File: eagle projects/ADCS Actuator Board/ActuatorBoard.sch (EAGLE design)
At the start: 256 parts, among them J4 OSTVN08A150, J5 OSTVN08A150, J6 OSTVN08A150, U10 TVS991, U11 BD621F-E2, U12 ADS7841E_2K5, U13 ADS7841E_2K5, U15 TLV9051IDCKR, U16 BD621F-E2, U17 DRV10970_MOTOR_DRIVERDRV10970, U18 DRV10970_MOTOR_DRIVERDRV10970, U19 TLV9051IDCKR, U20 DRV10970_MOTOR_DRIVERDRV10970, U21 TLV9051IDCKR, U22 BD621F-E2, U23 TLV9051IDCKR, U24 TLV9051IDCKR, U25 ADS7841E_2K5, U26 TLV9051IDCKR, U27 ADS7841E_2K5, U28 TLV9051IDCKR, U29 TLV9051IDCKR, U30 TLV9051IDCKR, U31 TLV9051IDCKR, U32 TLV9051IDCKR, U4 ADS7841E_2K5, U6 TLV9051IDCKR, U7 TVS991, U8 TVS991, U9 ADS7841E_2K5

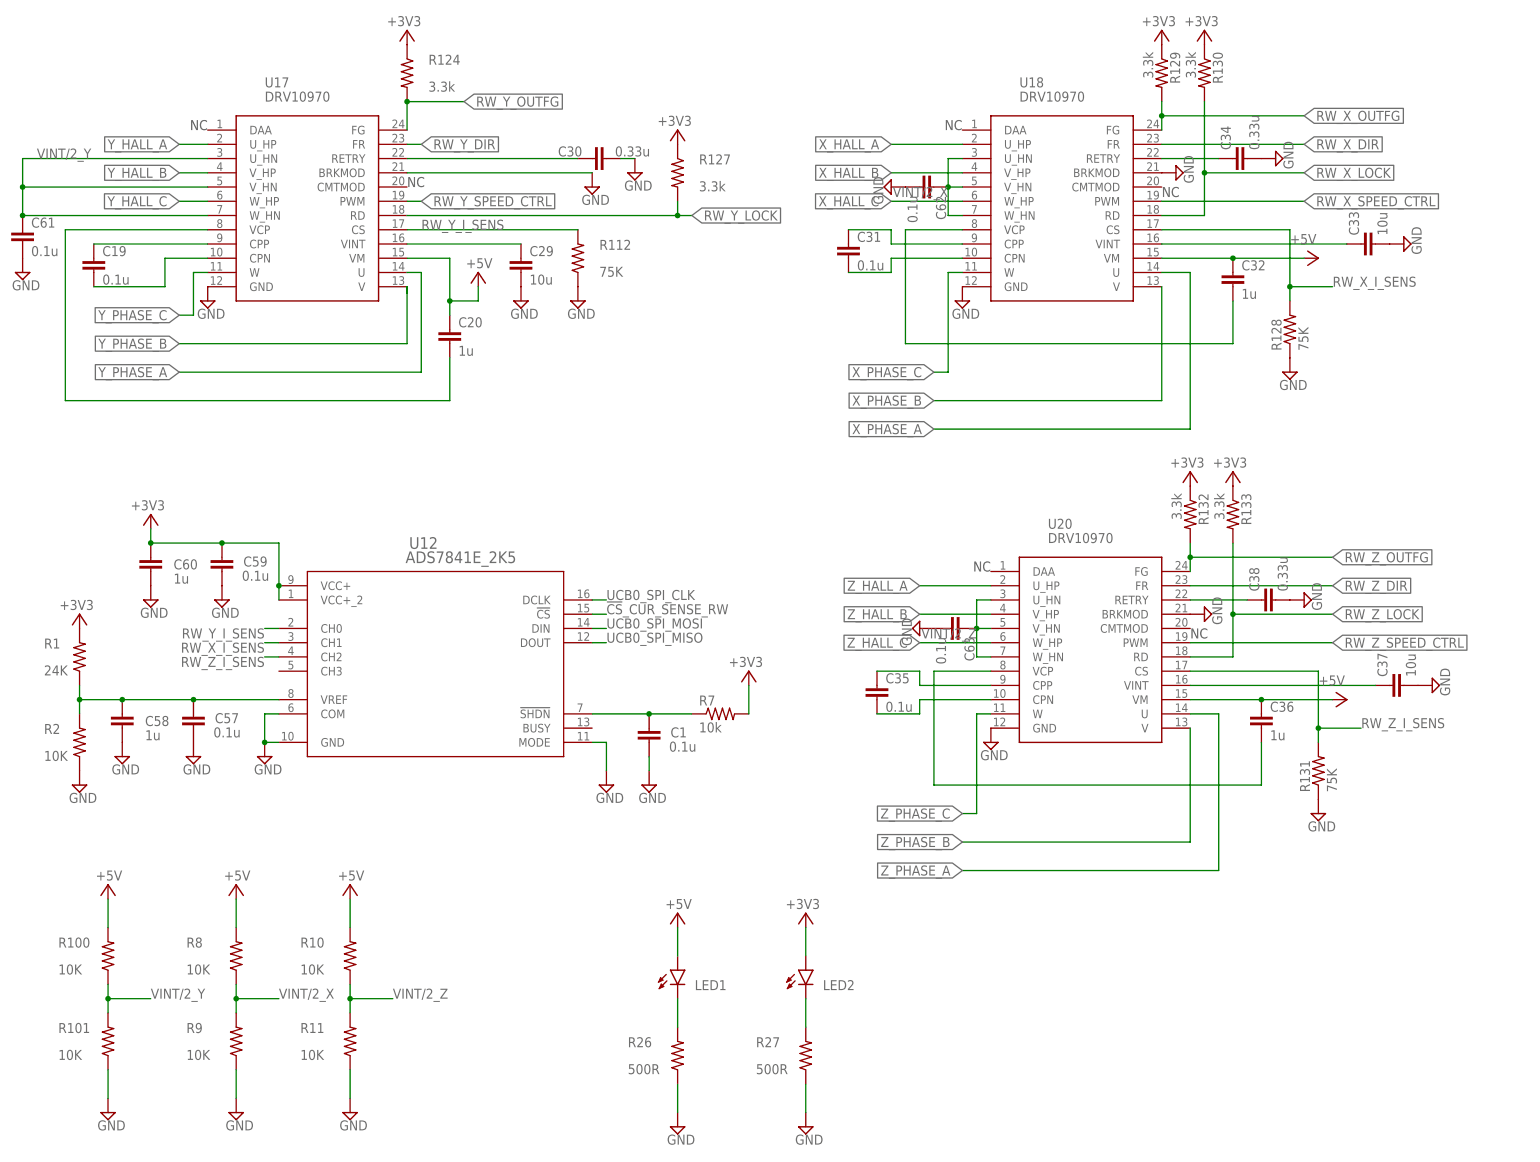
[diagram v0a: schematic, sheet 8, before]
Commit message: replaced 10u caps with 4.7u
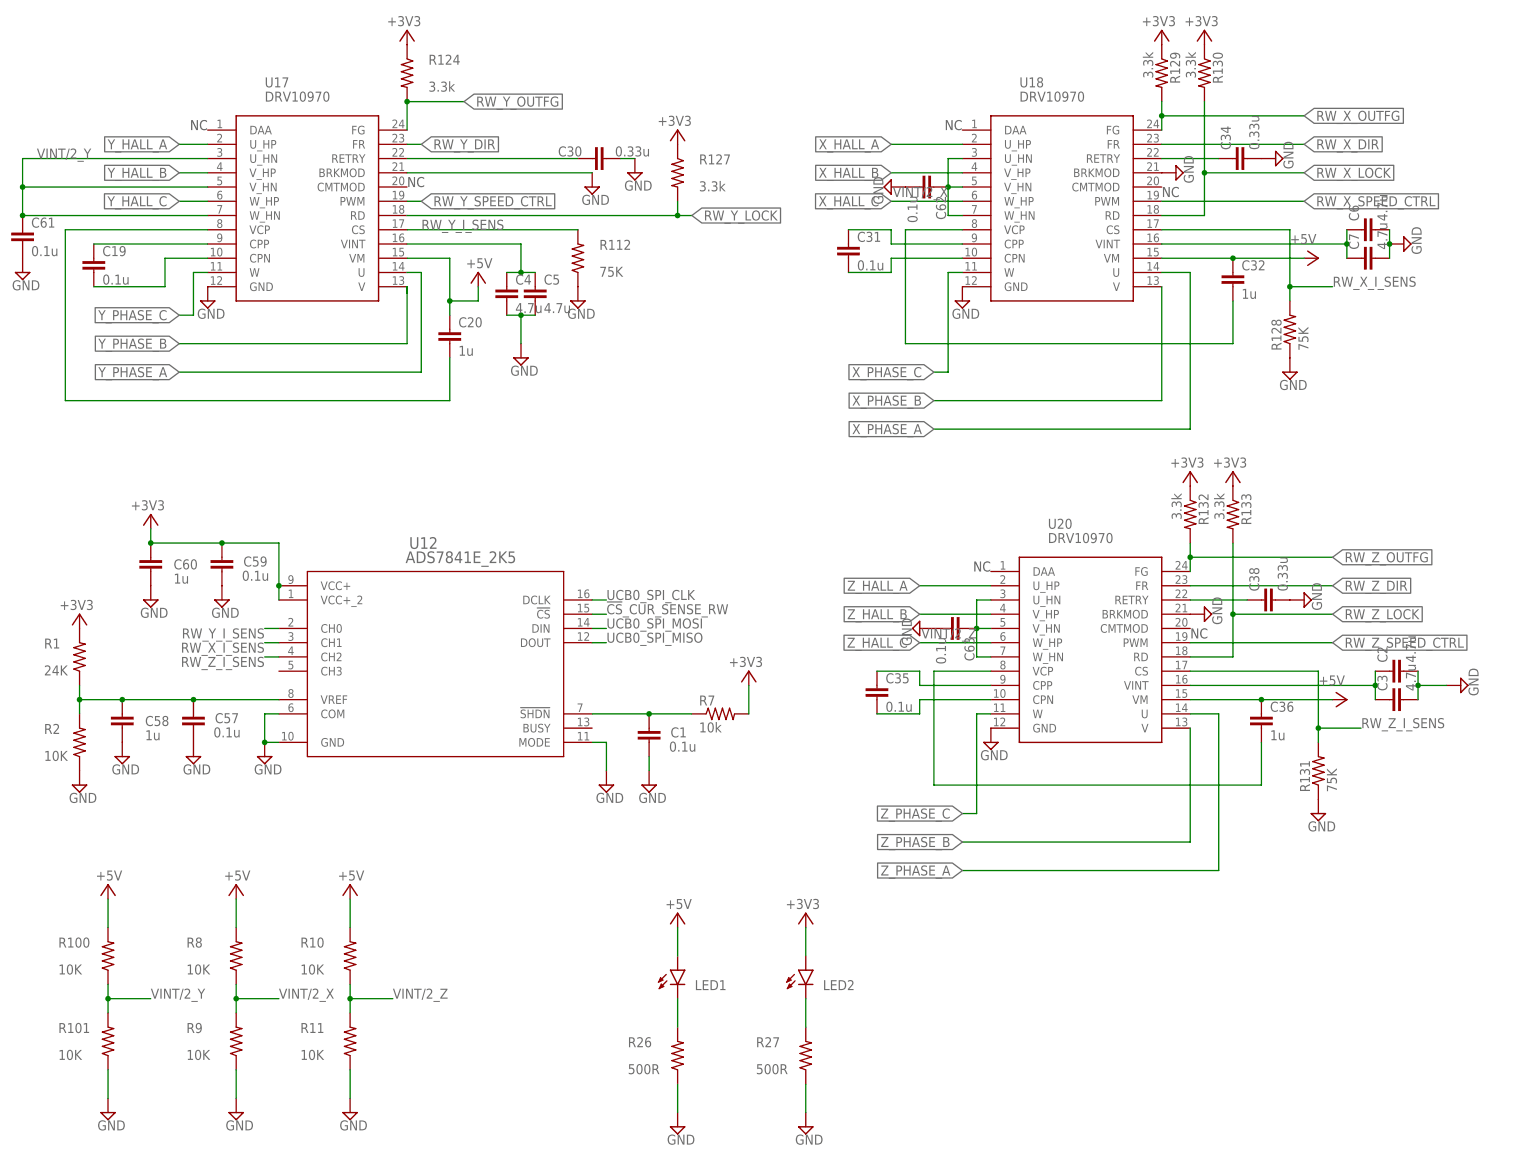
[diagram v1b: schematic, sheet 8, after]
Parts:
- removed C29, C33, C37: 10u, rcl:C-EUC0603
- added C2, C3, C4, C5, C6, C7: 4.7u, resistor:C-EUC0402
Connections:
- removed net N$28: J2.15
- net +3V3: now also J2.15
- net GND: now also C2.2, C3.2, C4.2, C5.2, C6.2, C7.2; no longer C29.2, C33.2, C37.2
- net N$26: now also C4.1, C5.1; no longer C29.1
- net N$42: now also C6.1, C7.1; no longer C33.1
- net N$53: now also C2.1, C3.1; no longer C37.1

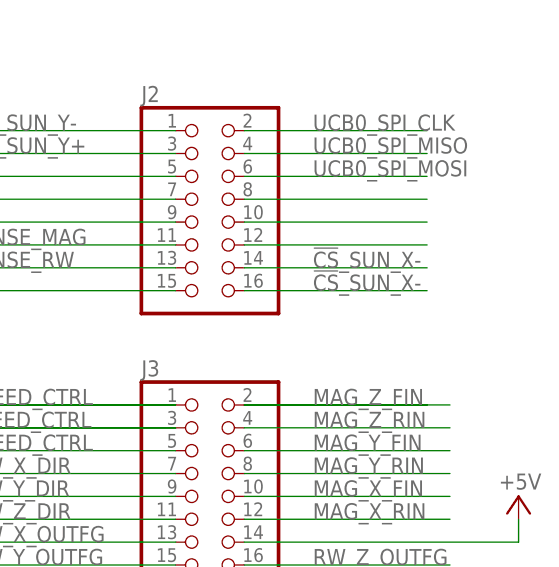
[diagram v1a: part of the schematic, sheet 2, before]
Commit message: laid out polygons for power plane
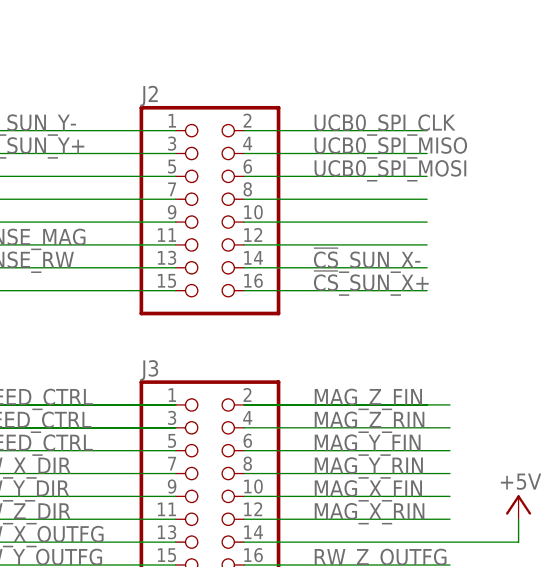
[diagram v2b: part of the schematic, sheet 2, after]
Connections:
- net !CS!_SUN_X+: now also J2.16
- net !CS!_SUN_X-: no longer J2.16
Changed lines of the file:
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@@
 <net name="!CS!_SUN_X-" class="0">
-<segment>
-<wire x1="185.42" y1="119.38" x2="165.1" y2="119.38" width="0.1524" layer="91" grouprefs="SENSOR_BOARD_CONNNECTOR"/>
-<pinref part="J2" gate="A" pin="16"/>
-<label x="172.72" y="119.38" size="1.778" layer="95" grouprefs="SENSOR_BOARD_CONNNECTOR"/>
-</segment>
 <segment>
 <pinref part="J2" gate="A" pin="14"/>
@@
 </segment>
 </net>
+<net name="!CS!_SUN_X+" class="0">
+<segment>
+<wire x1="185.42" y1="119.38" x2="165.1" y2="119.38" width="0.1524" layer="91" grouprefs="SENSOR_BOARD_CONNNECTOR"/>
+<pinref part="J2" gate="A" pin="16"/>
+<label x="172.72" y="119.38" size="1.778" layer="95" grouprefs="SENSOR_BOARD_CONNNECTOR"/>
+</segment>
+</net>

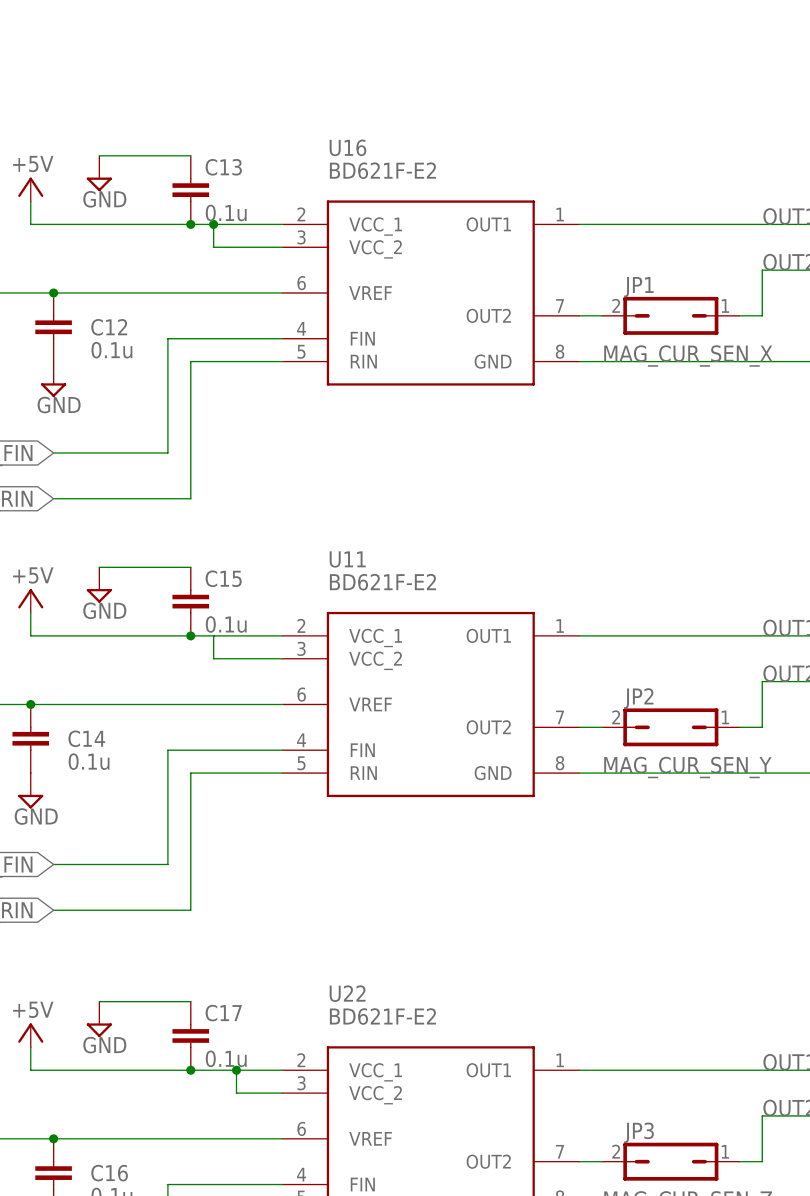
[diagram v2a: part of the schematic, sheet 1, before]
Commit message: updated footprint step models
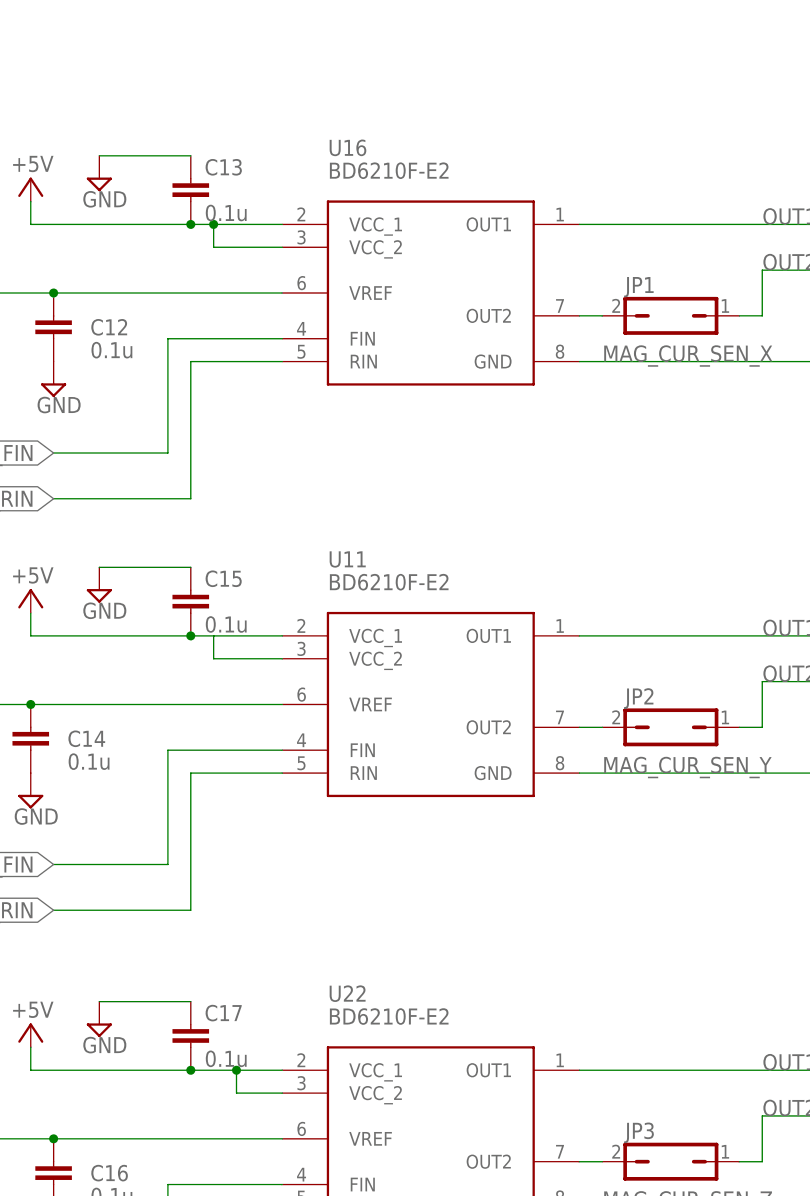
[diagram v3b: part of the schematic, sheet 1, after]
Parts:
- U11, U16, U22: value BD621F-E2 -> BD6210F-E2; device my_library:BD621F-E2 -> my_library:BD6210F-E2
